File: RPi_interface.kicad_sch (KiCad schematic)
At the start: 3 parts

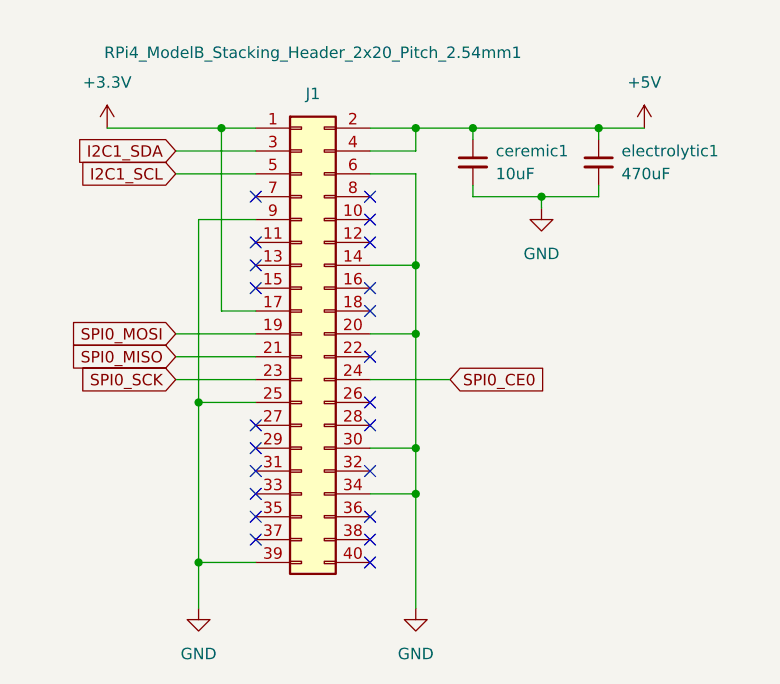
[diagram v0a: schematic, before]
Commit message: feat(power & programmer): Finished Schematic building. Now sourcing for parts.
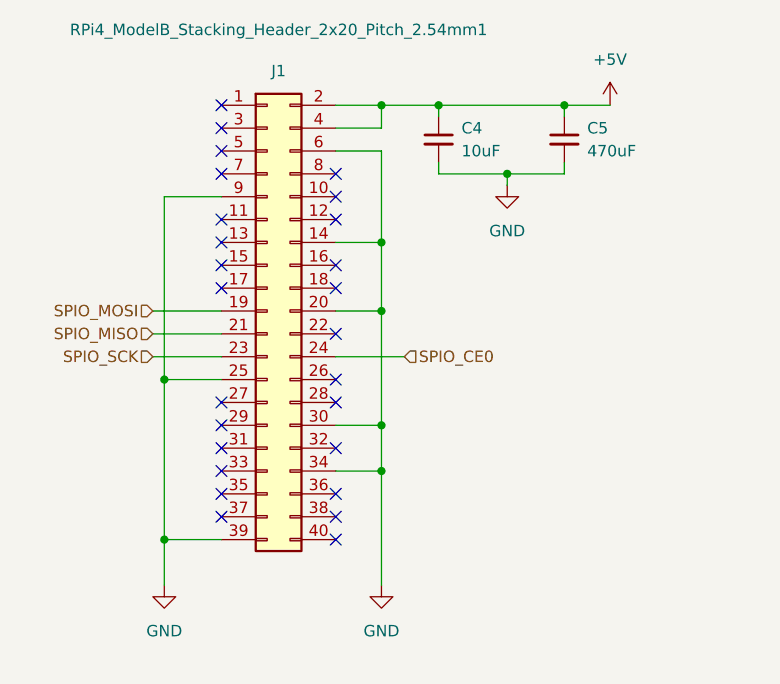
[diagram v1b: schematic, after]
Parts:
- renumbered ceremic1 to C4, electrolytic1 to C5
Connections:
- net +3.3V: no longer names the net of RPi4_ModelB_Stacking_Header_2x20_Pitch_2.54mm1.1 (3v3)
- net +3.3V: no longer RPi4_ModelB_Stacking_Header_2x20_Pitch_2.54mm1.17 (3v3)
- net I2C1_SCL: no longer names the net of RPi4_ModelB_Stacking_Header_2x20_Pitch_2.54mm1.5 (GPIO3)
- net I2C1_SDA: no longer names the net of RPi4_ModelB_Stacking_Header_2x20_Pitch_2.54mm1.3 (GPIO2)
- net SPI0_CE0 renamed SPIO_CE0
- net SPI0_MISO renamed SPIO_MISO
- net SPI0_MOSI renamed SPIO_MOSI
- net SPI0_SCK renamed SPIO_SCK
- no-connect marks 22 -> 26
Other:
- moved on the sheet: C4, C5, RPi4_ModelB_Stacking_Header_2x20_Pitch_2.54mm1
